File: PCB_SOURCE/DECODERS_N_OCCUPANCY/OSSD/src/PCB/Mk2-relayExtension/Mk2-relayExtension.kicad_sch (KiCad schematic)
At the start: 0 parts

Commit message: added some files, but mainly this is to update hex file of OSSD
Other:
- added sheet relay2 (relay.kicad_sch)
- added sheet relay3 (relay.kicad_sch)
- added sheet relay4 (relay.kicad_sch)
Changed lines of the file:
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@@
+		)
+	)
+	(sheet
+		(at 45.72 71.12)
+		(size 12.7 5.08)
+		(stroke
+			(width 0.1524)
+			(type solid)
+		)
+		(fill
+			(color 0 0 0 0.0000)
+		)
+		(property "Sheetname" "relay3"
+			(at 49.53 73.66 0)
+			(effects
+				(font
+					(size 1.27 1.27)
+				)
+				(justify left bottom)
+			)
+		)
+		(property "Sheetfile" "relay.kicad_sch"
+			(at 45.72 76.7846 0)
+			(effects
+				(font
+					(size 1.27 1.27)
+				)
+				(justify left top)
+			)
+		)
+		(instances
+			(project "Mk2-relayExtension"
+				(path "/e7280eb5-1386-47ea-974c-c755a08b04e7"
+					(page "4")
+				)
+			)
+		)
+	)
+	(sheet
+		(at 45.72 78.74)
+		(size 12.7 5.08)
+		(stroke
+			(width 0.1524)
+			(type solid)
+		)
+		(fill
+			(color 0 0 0 0.0000)
+		)
+		(property "Sheetname" "relay4"
+			(at 49.53 81.28 0)
+			(effects
+				(font
+					(size 1.27 1.27)
+				)
+				(justify left bottom)
+			)
+		)
+		(property "Sheetfile" "relay.kicad_sch"
+			(at 45.72 84.4046 0)
+			(effects
+				(font
+					(size 1.27 1.27)
+				)
+				(justify left top)
+			)
+		)
+		(instances
+			(project "Mk2-relayExtension"
+				(path "/e7280eb5-1386-47ea-974c-c755a08b04e7"
+					(page "5")
+				)
+			)
+		)
+	)
+	(sheet
+		(at 45.72 62.23)
+		(size 12.7 5.08)
+		(stroke
+			(width 0.1524)
+			(type solid)
+		)
+		(fill
+			(color 0 0 0 0.0000)
+		)
+		(property "Sheetname" "relay2"
+			(at 49.53 64.77 0)
+			(effects
+				(font
+					(size 1.27 1.27)
+				)
+				(justify left bottom)
+			)
+		)
+		(property "Sheetfile" "relay.kicad_sch"
+			(at 45.72 67.8946 0)
+			(effects
+				(font
+					(size 1.27 1.27)
+				)
+				(justify left top)
+			)
+		)
+		(instances
+			(project "Mk2-relayExtension"
+				(path "/e7280eb5-1386-47ea-974c-c755a08b04e7"
+					(page "3")
+				)
+			)
 		)
 	)

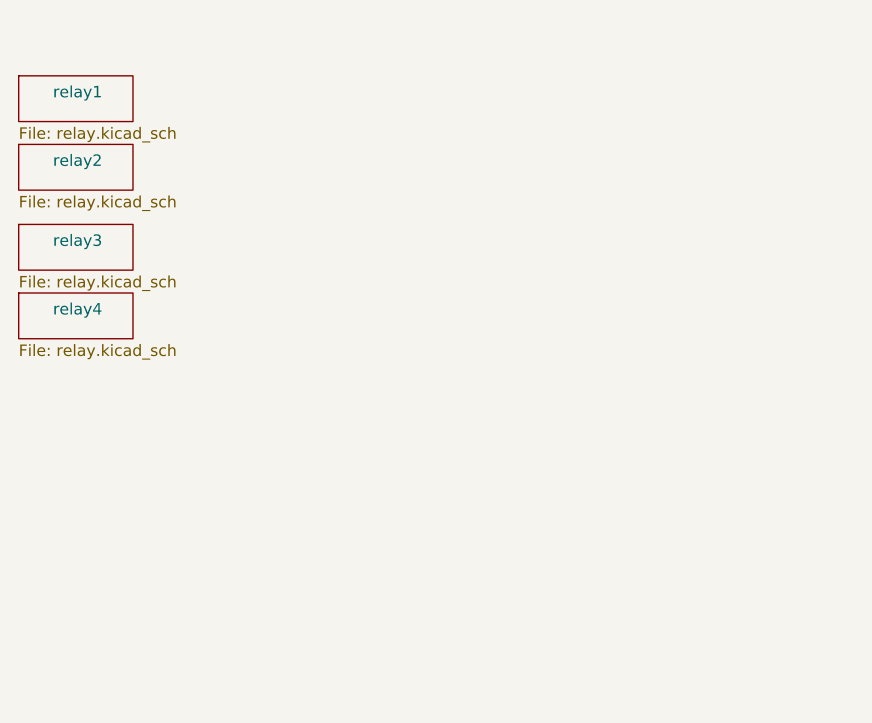
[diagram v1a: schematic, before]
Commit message: added some PCB designs
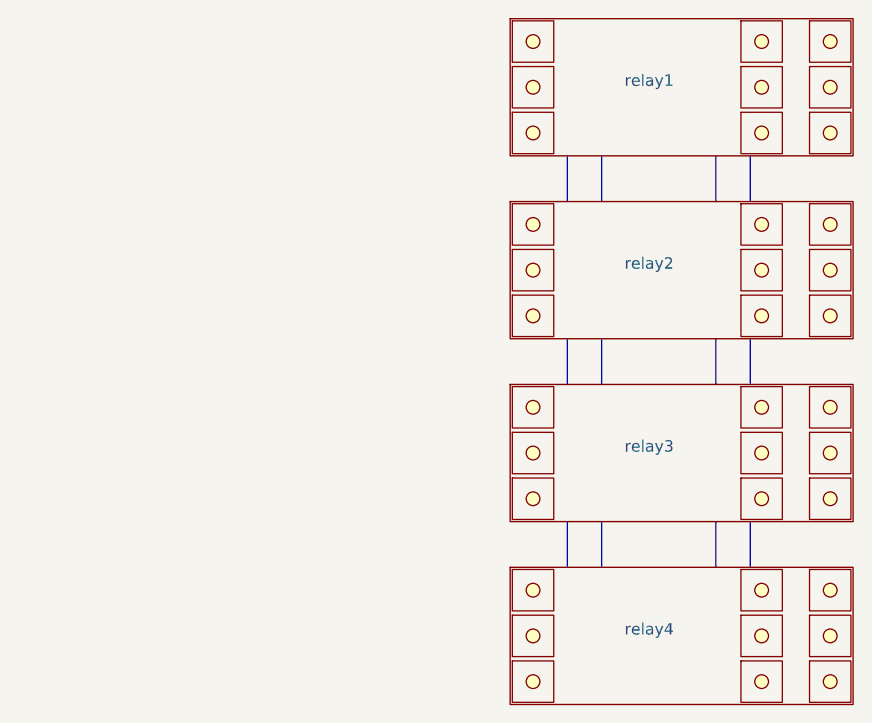
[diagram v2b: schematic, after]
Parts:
- added u1, u10, u11, u12, u13, u14, u15, u16, u17, u18, u19, u2, u20, u21, u22, u23, u24, u25, u26, u27, u28, u29, u3, u30, u31, u32, u33, u34, u35, u36, u4, u5, u6, u7, u8, u9: ~, symbol custom_kicad_lib_sk:screwterminal
